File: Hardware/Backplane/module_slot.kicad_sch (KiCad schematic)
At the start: 4 parts, among them J301 10018784-10201TLF, U201 SN74LVC2G66DCUR, U202 SN74LVC2G66DCUR, U203 SN74LVC2G66DCUR

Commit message: Adds more work on the backplane.
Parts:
- renumbered J301 to J701, U201 to U701, U202 to U702, U203 to U703
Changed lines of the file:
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@@
 		(dnp no)
 		(fields_autoplaced yes)
-		(property "Reference" "#PWR0208"
+		(property "Reference" "#PWR0708"
 			(at 228.6 123.19 0)
 			(effects
@@
 		(dnp no)
 		(fields_autoplaced yes)
-		(property "Reference" "#PWR0207"
+		(property "Reference" "#PWR0707"
 			(at 190.5 41.91 0)
 			(effects
@@
 		(on_board yes)
 		(dnp no)
-		(property "Reference" "#PWR0205"
+		(property "Reference" "#PWR0705"
 			(at 64.77 104.14 0)
 			(effects
@@
 		(dnp no)
 		(fields_autoplaced yes)
-		(property "Reference" "U202"
+		(property "Reference" "U702"
 			(at 209.55 68.58 0)
 			(effects
@@
 		(dnp no)
 		(fields_autoplaced yes)
-		(property "Reference" "#PWR0202"
+		(property "Reference" "#PWR0702"
 			(at 36.83 106.68 0)
 			(effects
@@
 		(dnp no)
 		(fields_autoplaced yes)
-		(property "Reference" "#PWR0204"
+		(property "Reference" "#PWR0704"
 			(at 66.04 116.84 0)
 			(effects
@@
 		(dnp no)
 		(fields_autoplaced yes)
-		(property "Reference" "J301"
+		(property "Reference" "J701"
 			(at 50.8 17.78 0)
 			(effects
@@
 		(dnp no)
 		(fields_autoplaced yes)
-		(property "Reference" "U203"
+		(property "Reference" "U703"
 			(at 209.55 93.98 0)
 			(effects
@@
 		(on_board yes)
 		(dnp no)
-		(property "Reference" "#PWR0201"
+		(property "Reference" "#PWR0701"
 			(at 36.83 104.14 0)
 			(effects
@@
 		(dnp no)
 		(fields_autoplaced yes)
-		(property "Reference" "#PWR0203"
+		(property "Reference" "#PWR0703"
 			(at 35.56 116.84 0)
 			(effects
@@
 		(dnp no)
 		(fields_autoplaced yes)
-		(property "Reference" "U201"
+		(property "Reference" "U701"
 			(at 209.55 43.18 0)
 			(effects
@@
 		(dnp no)
 		(fields_autoplaced yes)
-		(property "Reference" "#PWR0206"
+		(property "Reference" "#PWR0706"
 			(at 64.77 106.68 0)
 			(effects

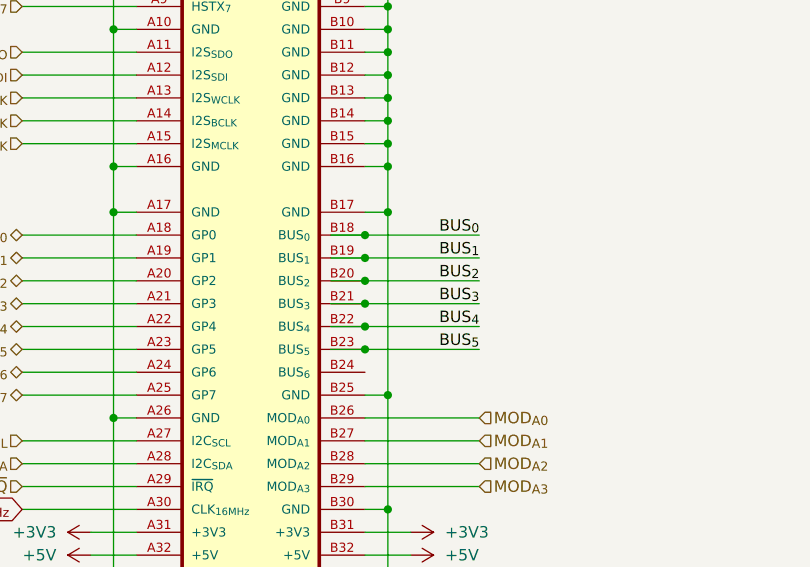
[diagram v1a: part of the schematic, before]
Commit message: Updates Expansion Bay Pinout
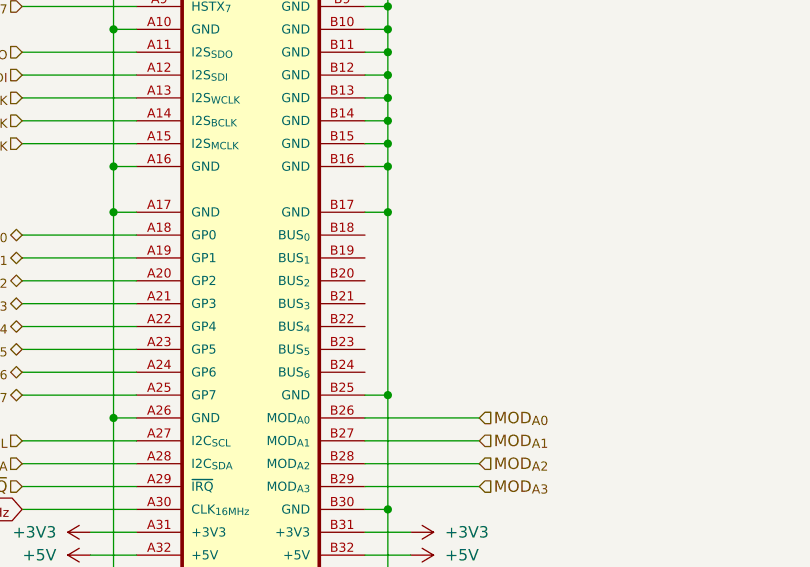
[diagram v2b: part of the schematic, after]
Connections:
- net BUS_{0}: no longer J701.B18 (BUS_{0})
- net BUS_{1}: no longer J701.B19 (BUS_{1})
- net BUS_{2}: no longer J701.B20 (BUS_{2})
- net BUS_{3}: no longer J701.B21 (BUS_{3})
- net BUS_{4}: no longer J701.B22 (BUS_{4})
- net BUS_{5}: no longer J701.B23 (BUS_{5})
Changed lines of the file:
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@@
-	)
-	(junction
-		(at 63.5 83.82)
-		(diameter 0)
-		(color 0 0 0 0)
 	)
 	(junction
@@
 	)
 	(junction
-		(at 63.5 78.74)
-		(diameter 0)
-		(color 0 0 0 0)
-	)
-	(junction
 		(at 35.56 68.58)
 		(diameter 0)
@@
 	)
 	(junction
-		(at 63.5 71.12)
-		(diameter 0)
-		(color 0 0 0 0)
-	)
-	(junction
 		(at 66.04 33.02)
 		(diameter 0)
@@
 	)
 	(junction
-		(at 63.5 81.28)
-		(diameter 0)
-		(color 0 0 0 0)
-	)
-	(junction
-		(at 63.5 76.2)
-		(diameter 0)
-		(color 0 0 0 0)
-	)
-	(junction
 		(at 66.04 101.6)
 		(diameter 0)
@@
 	)
 	(junction
-		(at 63.5 73.66)
-		(diameter 0)
-		(color 0 0 0 0)
-	)
-	(junction
 		(at 66.04 48.26)
 		(diameter 0)
@@
 	(wire
 		(pts
-			(xy 63.5 76.2) (xy 76.2 76.2)
-		)
-		(stroke
-			(width 0)
-			(type default)
-		)
-	)
-	(wire
-		(pts
 			(xy 35.56 25.4) (xy 35.56 48.26)
 		)
@@
 	(wire
 		(pts
-			(xy 59.69 76.2) (xy 63.5 76.2)
-		)
-		(stroke
-			(width 0)
-			(type default)
-		)
-	)
-	(wire
-		(pts
 			(xy 25.4 78.74) (xy 38.1 78.74)
 		)
@@
 	(wire
 		(pts
-			(xy 63.5 81.28) (xy 76.2 81.28)
-		)
-		(stroke
-			(width 0)
-			(type default)
-		)
-	)
-	(wire
-		(pts
 			(xy 227.33 105.41) (xy 231.14 105.41)
 		)
@@
 	(wire
 		(pts
-			(xy 63.5 83.82) (xy 76.2 83.82)
-		)
-		(stroke
-			(width 0)
-			(type default)
-		)
-	)
-	(wire
-		(pts
 			(xy 227.33 80.01) (xy 231.14 80.01)
 		)
@@
 	(wire
 		(pts
-			(xy 63.5 71.12) (xy 76.2 71.12)
-		)
-		(stroke
-			(width 0)
-			(type default)
-		)
-	)
-	(wire
-		(pts
 			(xy 66.04 40.64) (xy 63.5 40.64)
 		)
@@
 	(wire
 		(pts
-			(xy 63.5 73.66) (xy 76.2 73.66)
-		)
-		(stroke
-			(width 0)
-			(type default)
-		)
-	)
-	(wire
-		(pts
 			(xy 63.5 27.94) (xy 66.04 27.94)
 		)
@@
 	(wire
 		(pts
-			(xy 59.69 78.74) (xy 63.5 78.74)
-		)
-		(stroke
-			(width 0)
-			(type default)
-		)
-	)
-	(wire
-		(pts
 			(xy 66.04 48.26) (xy 66.04 45.72)
 		)
@@
 	(wire
 		(pts
-			(xy 59.69 73.66) (xy 63.5 73.66)
-		)
-		(stroke
-			(width 0)
-			(type default)
-		)
-	)
-	(wire
-		(pts
 			(xy 25.4 81.28) (xy 38.1 81.28)
 		)
@@
 	(wire
 		(pts
-			(xy 59.69 81.28) (xy 63.5 81.28)
-		)
-		(stroke
-			(width 0)
-			(type default)
-		)
-	)
-	(wire
-		(pts
 			(xy 38.1 25.4) (xy 35.56 25.4)
 		)
@@
 	(wire
 		(pts
-			(xy 59.69 71.12) (xy 63.5 71.12)
-		)
-		(stroke
-			(width 0)
-			(type default)
-		)
-	)
-	(wire
-		(pts
 			(xy 227.33 114.3) (xy 228.6 114.3)
 		)
@@
 	(wire
 		(pts
-			(xy 63.5 78.74) (xy 76.2 78.74)
-		)
-		(stroke
-			(width 0)
-			(type default)
-		)
-	)
-	(wire
-		(pts
 			(xy 227.33 57.15) (xy 231.14 57.15)
 		)
@@
 			(width 0)
 			(type default)
-		)
-	)
-	(wire
-		(pts
-			(xy 59.69 83.82) (xy 63.5 83.82)
-		)
-		(stroke
-			(width 0)
-			(type default)
-		)
-	)
-	(label "BUS_{3}"
-		(at 76.2 78.74 180)
-		(fields_autoplaced yes)
-		(effects
-			(font
-				(size 1.27 1.27)
-			)
-			(justify right bottom)
 		)
 	)
@@
 		)
 	)
-	(label "BUS_{1}"
-		(at 76.2 73.66 180)
-		(fields_autoplaced yes)
-		(effects
-			(font
-				(size 1.27 1.27)
-			)
-			(justify right bottom)
-		)
-	)
 	(label "BUS_{2}"
 		(at 181.61 80.01 0)
@@
 		)
 	)
-	(label "BUS_{4}"
-		(at 76.2 81.28 180)
-		(fields_autoplaced yes)
-		(effects
-			(font
-				(size 1.27 1.27)
-			)
-			(justify right bottom)
-		)
-	)
 	(label "BUS_EN_{2}"
 		(at 181.61 86.36 0)
@@
 		)
 	)
-	(label "BUS_{5}"
-		(at 76.2 83.82 180)
-		(fields_autoplaced yes)
-		(effects
-			(font
-				(size 1.27 1.27)
-			)
-			(justify right bottom)
-		)
-	)
 	(label "BUS_{3}"
 		(at 181.61 82.55 0)
@@
 		)
 	)
-	(label "BUS_{2}"
-		(at 76.2 76.2 180)
-		(fields_autoplaced yes)
-		(effects
-			(font
-				(size 1.27 1.27)
-			)
-			(justify right bottom)
-		)
-	)
 	(label "BUS_EN_{3}"
 		(at 181.61 88.9 0)
@@
 		)
 	)
-	(label "BUS_{0}"
-		(at 76.2 71.12 180)
-		(fields_autoplaced yes)
-		(effects
-			(font
-				(size 1.27 1.27)
-			)
-			(justify right bottom)
-		)
-	)

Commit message: Improves Backplane Schematic a lot
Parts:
- removed U701, U702, U703: SN74LVC2G66DCUR, Home Computer:SOP50P310X90-8N, symbol Home Computer:SN74LVC2G66DCUR
- added R201, R202, R203: 10, Resistor_SMD:R_0603_1608Metric, symbol Device:R_Small
- added R204, R205, R206, R207, R210, R211, R212: 1K, Resistor_SMD:R_0603_1608Metric, symbol Device:R_Small
- added R208, R209: 4K7, Resistor_SMD:R_0603_1608Metric, symbol Device:R
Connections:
- net +3V3: now also J701.A3 (+3V3), R201.1, R208.1, R209.1; no longer J701.A31 (+3V3), J701.B31 (+3V3)
- net +5V: now also J701.B7 (+5V), R203.1; no longer J701.A32 (+5V), J701.B32 (+5V)
- net GND: now also J701.A12 (GND), J701.A14 (GND), J701.A32 (GND), J701.A4 (GND), J701.B18 (GND), J701.B21 (GND), J701.B24 (GND), J701.B26 (GND), J701.B29 (GND), J701.B32 (GND); no longer J701.A10 (GND), J701.A16 (GND), J701.A17 (GND), J701.A26 (GND), J701.B10 (GND), J701.B11 (GND), J701.B13 (GND), J701.B14 (GND), J701.B16 (GND), J701.B17 (GND), J701.B2 (GND), J701.B25 (GND), J701.B3 (GND), J701.B30 (GND), J701.B4 (GND), J701.B5 (GND), J701.B6 (GND), J701.B7 (GND), J701.B9 (GND)
- net GP_{0}: now also J701.A15 (GP0); no longer J701.A18 (GP0)
- net GP_{1}: now also J701.A16 (GP1); no longer J701.A19 (GP1)
- net GP_{2}: now also J701.A17 (GP2); no longer J701.A20 (GP2)
- net GP_{3}: now also J701.A18 (GP3); no longer J701.A21 (GP3)
- net GP_{4}: now also J701.A19 (GP4); no longer J701.A22 (GP4)
- net GP_{5}: now also J701.A20 (GP5); no longer J701.A23 (GP5)
- net GP_{6}: now also J701.A21 (GP6); no longer J701.A24 (GP6)
- net GP_{7}: now also J701.A22 (GP7); no longer J701.A25 (GP7)
- net HSTX_{0}: now also J701.B13 (HSTX_{0}); no longer J701.A2 (HSTX_{0})
- net HSTX_{1}: now also J701.B14 (HSTX_{1}); no longer J701.A3 (HSTX_{1})
- net HSTX_{2}: now also J701.B16 (HSTX_{2}); no longer J701.A4 (HSTX_{2})
- net HSTX_{3}: now also J701.B17 (HSTX_{3}); no longer J701.A5 (HSTX_{3})
- net HSTX_{4}: now also J701.B19 (HSTX_{4}); no longer J701.A6 (HSTX_{4})
- net HSTX_{5}: now also J701.B20 (HSTX_{5}); no longer J701.A7 (HSTX_{5})
- net HSTX_{6}: now also J701.B22 (HSTX_{6}); no longer J701.A8 (HSTX_{6})
- net HSTX_{7}: now also J701.B23 (HSTX_{7}); no longer J701.A9 (HSTX_{7})
- net I2C_{SCL}: now also J701.A9 (I²C_{SCL}), R208.2; no longer J701.A27 (I2C_{SCL})
- net I2C_{SDA}: now also J701.A10 (I²C_{SDA}), R209.2; no longer J701.A28 (I2C_{SDA})
- net I2S_{BCLK}: now also J701.B28 (I²S_{BCLK}); no longer J701.A14 (I2S_{BCLK})
- net I2S_{MCLK}: now also J701.B25 (I²S_{MCLK}); no longer J701.A15 (I2S_{MCLK})
- net I2S_{SDI}: now also J701.B30 (I²S_{SDIN}); no longer J701.A12 (I2S_{SDI})
- net I2S_{SDO}: now also J701.B31 (I²S_{SDOUT}); no longer J701.A11 (I2S_{SDO})
- net MOD_{A0}: now also R204.1; no longer J701.B26 (MOD_{A0})
- net MOD_{A1}: now also R205.1; no longer J701.B27 (MOD_{A1})
- net MOD_{A2}: now also R206.1; no longer J701.B28 (MOD_{A2})
- net MOD_{A3}: now also R207.1; no longer J701.B29 (MOD_{A3})
- net ~{IRQ}: now also J701.A11 (~{IRQ}); no longer J701.A29 (~{IRQ})
- net CLK_{16MHz}: no longer names the net of J701.A30 (RES)
- net I2S_{LRCLK} renamed CLOCK
- new net: J701.A8 (SLOT_{A3}), R207.2
- new net: J701.B10 (~{SLOT_{AUDIO}}), R210.1
- new net: J701.A2 (+3V3_{RI}), R201.2
- new net: J701.B6 (+5V_{RI}), R203.2
- new net: J701.A5 (SLOT_{A0}), R204.2
- new net: J701.B11 (~{SLOT_{VIDEO}}), R211.1
- new net: J701.A6 (SLOT_{A1}), R205.2
- new net: J701.A7 (SLOT_{A2}), R206.2
- new net: J701.B2 (+12V_{RI}), R202.2
- new net: J701.B9 (~{PDET}), R212.1
- new net +12V: J701.B3 (+12V), J701.B4 (+12V), J701.B5 (+12V), R202.1
- new net I2S_{WCLK}: J701.B27 (I²S_{WCLK})
- new net SLOT_{AUDIO}: R210.2
- new net SLOT_{PRESENT}: R212.2
- new net SLOT_{VIDEO}: R211.2
- new net ~{G_RESET}: J701.A31 (~{RESET})
- no-connect marks 0 -> 8
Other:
- added sheet Reset Gate1 (reset_gate.kicad_sch)

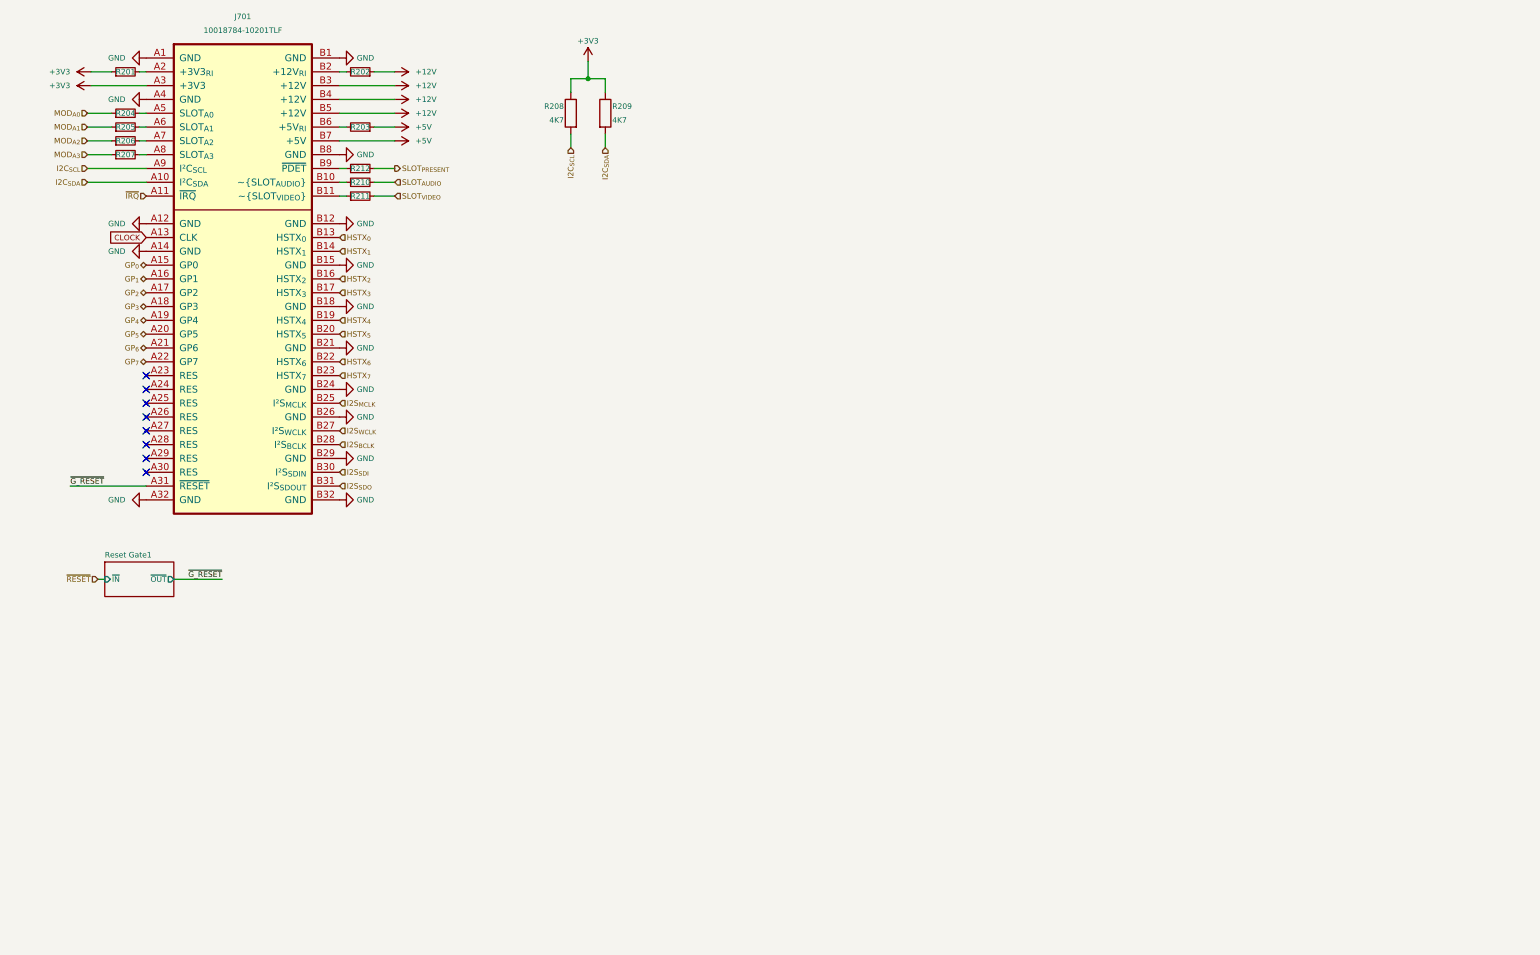
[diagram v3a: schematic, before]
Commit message: Some work on the backplane schematics: Improves module locality
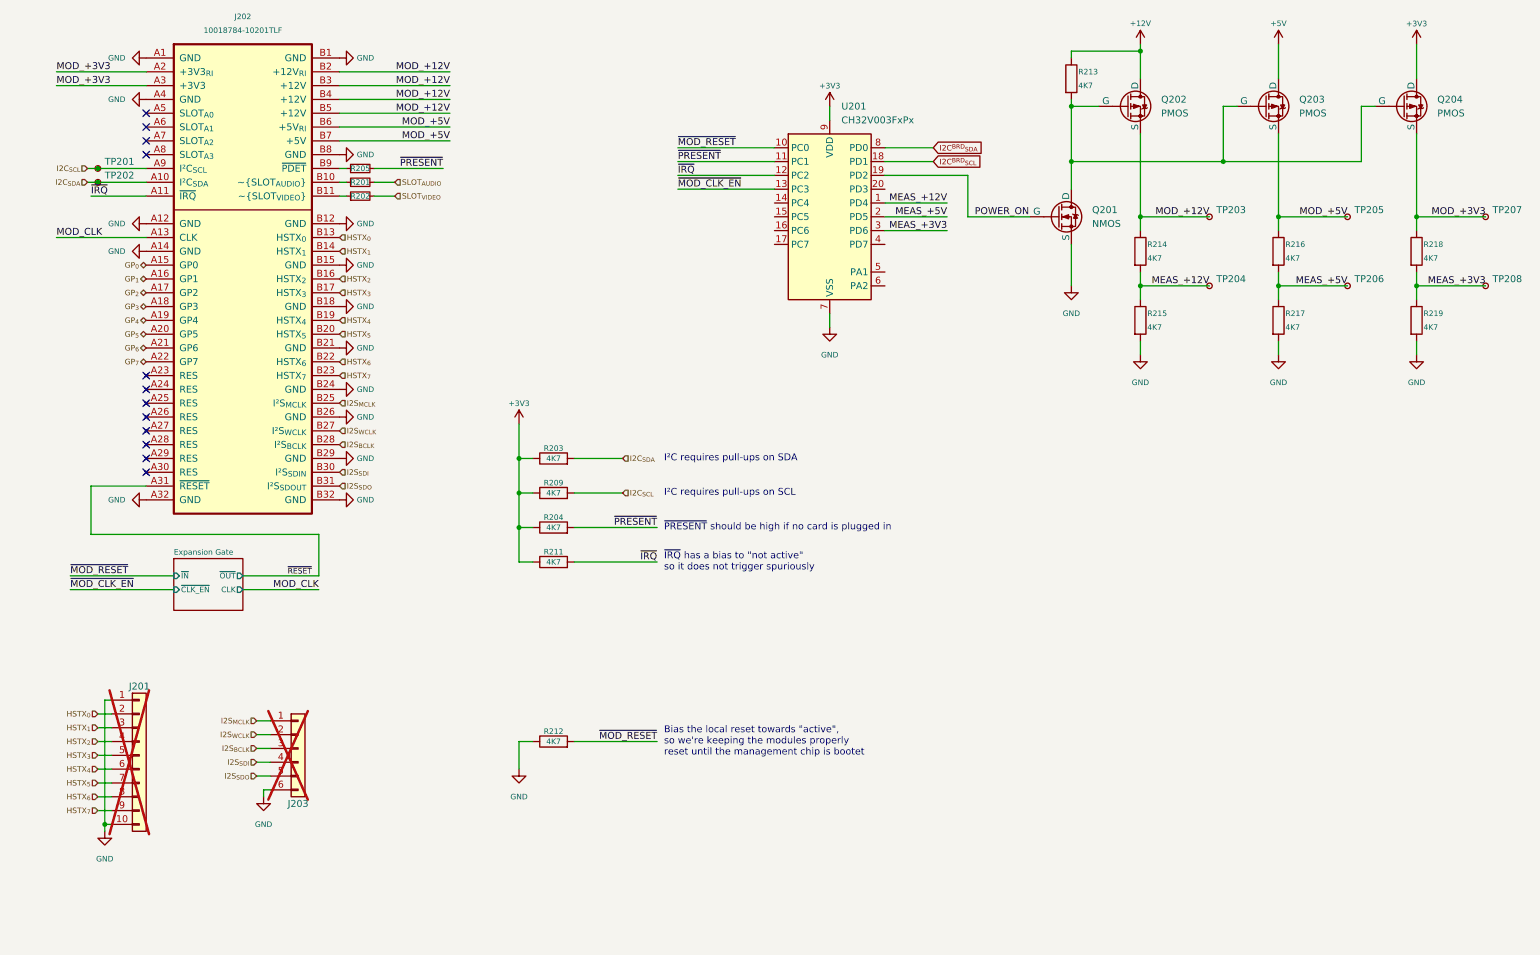
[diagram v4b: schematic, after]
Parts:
- removed R203: 10, Resistor_SMD:R_0603_1608Metric, symbol Device:R_Small
- removed R204, R205, R206, R207, R210, R211: 1K, Resistor_SMD:R_0603_1608Metric, symbol Device:R_Small
- removed R208: 4K7, Resistor_SMD:R_0603_1608Metric, symbol Device:R
- added J201: Conn_01x10, Connector_Molex:Molex_PicoBlade_53047-1010_1x10_P1.25mm_Vertical, symbol Connector_Generic:Conn_01x10
- added J203: Conn_01x06, Connector_Molex:Molex_PicoBlade_53047-0610_1x06_P1.25mm_Vertical, symbol Connector_Generic:Conn_01x06
- added Q201: NMOS, Package_TO_SOT_SMD:SOT-23, symbol Simulation_SPICE:NMOS
- added Q202, Q203, Q204: PMOS, Package_TO_SOT_SMD:SOT-23, symbol Simulation_SPICE:PMOS
- added R203, R204, R211, R212, R213, R214, R215, R216, R217, R218, R219: 4K7, Resistor_SMD:R_0603_1608Metric, symbol Device:R
- added TP201, TP202, TP203, TP204, TP205, TP206, TP207, TP208: TestPoint_Small, TestPoint:TestPoint_Pad_D1.0mm, symbol Connector:TestPoint_Small
- added U201: CH32V003FxPx, Package_SO:TSSOP-20_4.4x6.5mm_P0.65mm, symbol MCU_WCH_CH32V0:CH32V003FxPx
- R201, R202: value 10 -> 1K
- renumbered J701 to J202, R212 to R205
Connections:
- net ~{G_RESET} is gone; now on net ~{RESET}: J202.A31 (~{RESET})
- net +12V: now also Q202.1 (D), R213.1; no longer J202.B3 (+12V), J202.B4 (+12V), J202.B5 (+12V), R202.1
- net +3V3: now also Q204.1 (D), R203.1, R204.1, R211.1, U201.9 (VDD); no longer J202.A3 (+3V3), R201.1
- net +5V: now also Q203.1 (D); no longer J202.B7 (+5V)
- net GND: now also J201.1 (Pin_1), J201.10 (Pin_10), J203.6 (Pin_6), Q201.3 (S), R212.1, R215.2, R217.2, R219.2, U201.7 (VSS)
- net HSTX_{0}: now also J201.2 (Pin_2)
- net HSTX_{1}: now also J201.3 (Pin_3)
- net HSTX_{2}: now also J201.4 (Pin_4)
- net HSTX_{3}: now also J201.5 (Pin_5)
- net HSTX_{4}: now also J201.6 (Pin_6)
- net HSTX_{5}: now also J201.7 (Pin_7)
- net HSTX_{6}: now also J201.8 (Pin_8)
- net HSTX_{7}: now also J201.9 (Pin_9)
- net I2C_{SCL}: now also R209.2, TP201.1
- net I2C_{SDA}: now also R203.2, TP202.1; no longer R209.2
- net I2S_{BCLK}: now also J203.3 (Pin_3)
- net I2S_{MCLK}: now also J203.1 (Pin_1)
- net I2S_{SDI}: now also J203.4 (Pin_4)
- net I2S_{SDO}: now also J203.5 (Pin_5)
- net I2S_{WCLK}: now also J203.2 (Pin_2)
- net SLOT_{AUDIO}: now also R201.2
- net SLOT_{VIDEO}: now also R202.2
- net ~{IRQ}: now also R211.2, U201.12 (PC2)
- net at J202.B10 (~{SLOT_{AUDIO}}): now also R201.1
- net MOD_+3V3: now reaches J202.A2 (+3V3_{RI})
- net MOD_+3V3: now also J202.A3 (+3V3), Q204.3 (S), R218.1, TP207.1; no longer R201.2
- net MOD_+5V: now reaches J202.B6 (+5V_{RI})
- net MOD_+5V: now also J202.B7 (+5V), Q203.3 (S), R216.1, TP205.1
- net at J202.B11 (~{SLOT_{VIDEO}}): now also R202.1
- net MOD_+12V: now reaches J202.B2 (+12V_{RI})
- net MOD_+12V: now also J202.B3 (+12V), J202.B4 (+12V), J202.B5 (+12V), Q202.3 (S), R214.1, TP203.1; no longer R202.2
- net CLOCK renamed MOD_CLK
- net SLOT_{PRESENT} renamed ~{PRESENT}
- net ~{PRESENT}: now also R204.2, U201.11 (PC1)
- new net: Q201.1 (D), Q202.2 (G), Q203.2 (G), Q204.2 (G), R213.2
- new net I2C^{BRD}_{SCL}: U201.18 (PD1)
- new net I2C^{BRD}_{SDA}: U201.8 (PD0)
- new net MEAS_+12V: R214.2, R215.1, TP204.1, U201.1 (PD4)
- new net MEAS_+3V3: R218.2, R219.1, TP208.1, U201.3 (PD6)
- new net MEAS_+5V: R216.2, R217.1, TP206.1, U201.2 (PD5)
- new net POWER_ON: Q201.2 (G), U201.19 (PD2)
- new net ~{MOD_CLK_EN}: U201.13 (PC3)
- new net ~{MOD_RESET}: R212.2, U201.10 (PC0)
- no-connect marks 8 -> 12
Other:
- sheet Reset Gate1 renamed Expansion Gate
- sheet Expansion Gate ports: added CLK, ~{CLK_EN}; removed none
- note added: "Bias the local reset towards "active", so we're keeping the modules properly reset until the management chip is bootet"
- note added: "I²C requires pull-ups on SCL"
- note added: "I²C requires pull-ups on SDA"
- note added: "~{IRQ} has a bias to "not active" so it does not trigger spuriously"
- note added: "~{PRESENT} should be high if no card is plugged in"
